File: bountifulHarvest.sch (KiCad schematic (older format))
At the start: 0 parts

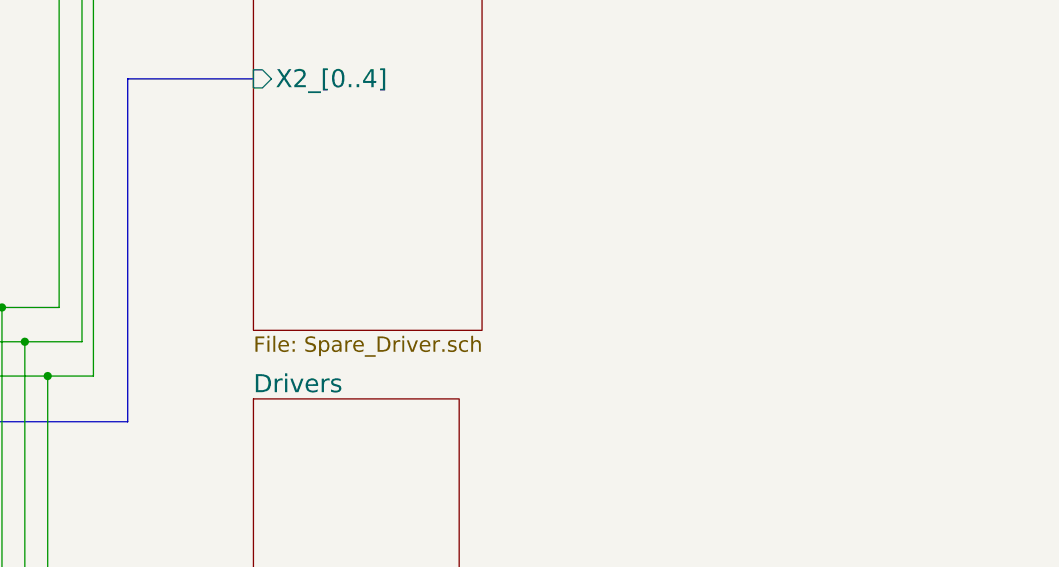
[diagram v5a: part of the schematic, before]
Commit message: Found error in stepper driver supply
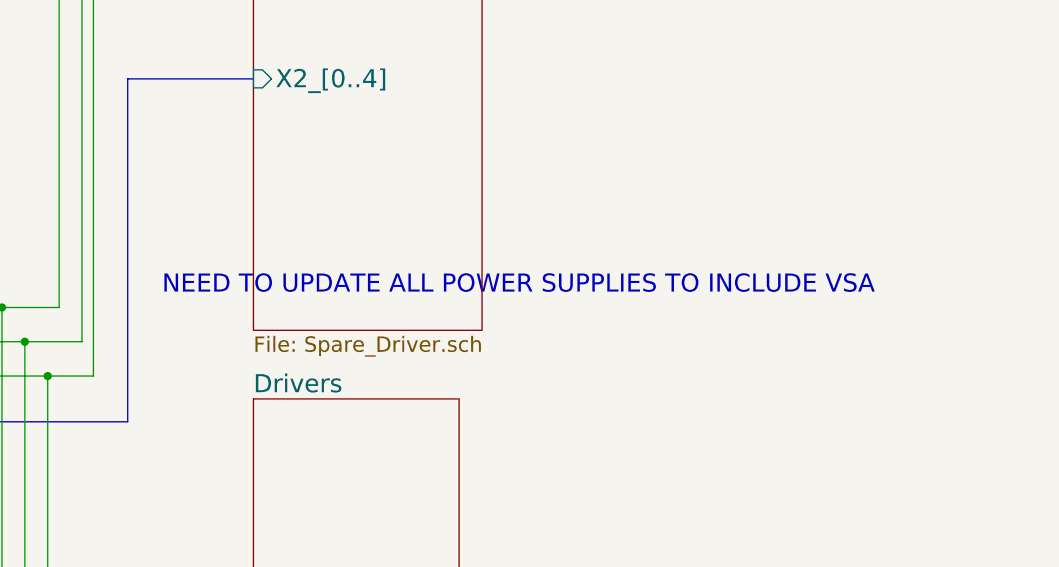
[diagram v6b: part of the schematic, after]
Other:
- note added: "NEED TO UPDATE ALL POWER SUPPLIES TO INCLUDE VSA"
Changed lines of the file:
@@
 EESchema Schematic File Version 4
-LIBS:bountifulHarvest-cache
-EELAYER 26 0
+EELAYER 30 0
 EELAYER END
 $Descr A4 11693 8268
@@
 Wire Wire Line
 	3850 6950 4350 6950
+Text Notes 9700 2750 0    79   ~ 0
+NEED TO UPDATE ALL POWER SUPPLIES TO INCLUDE VSA
 $EndSCHEMATC

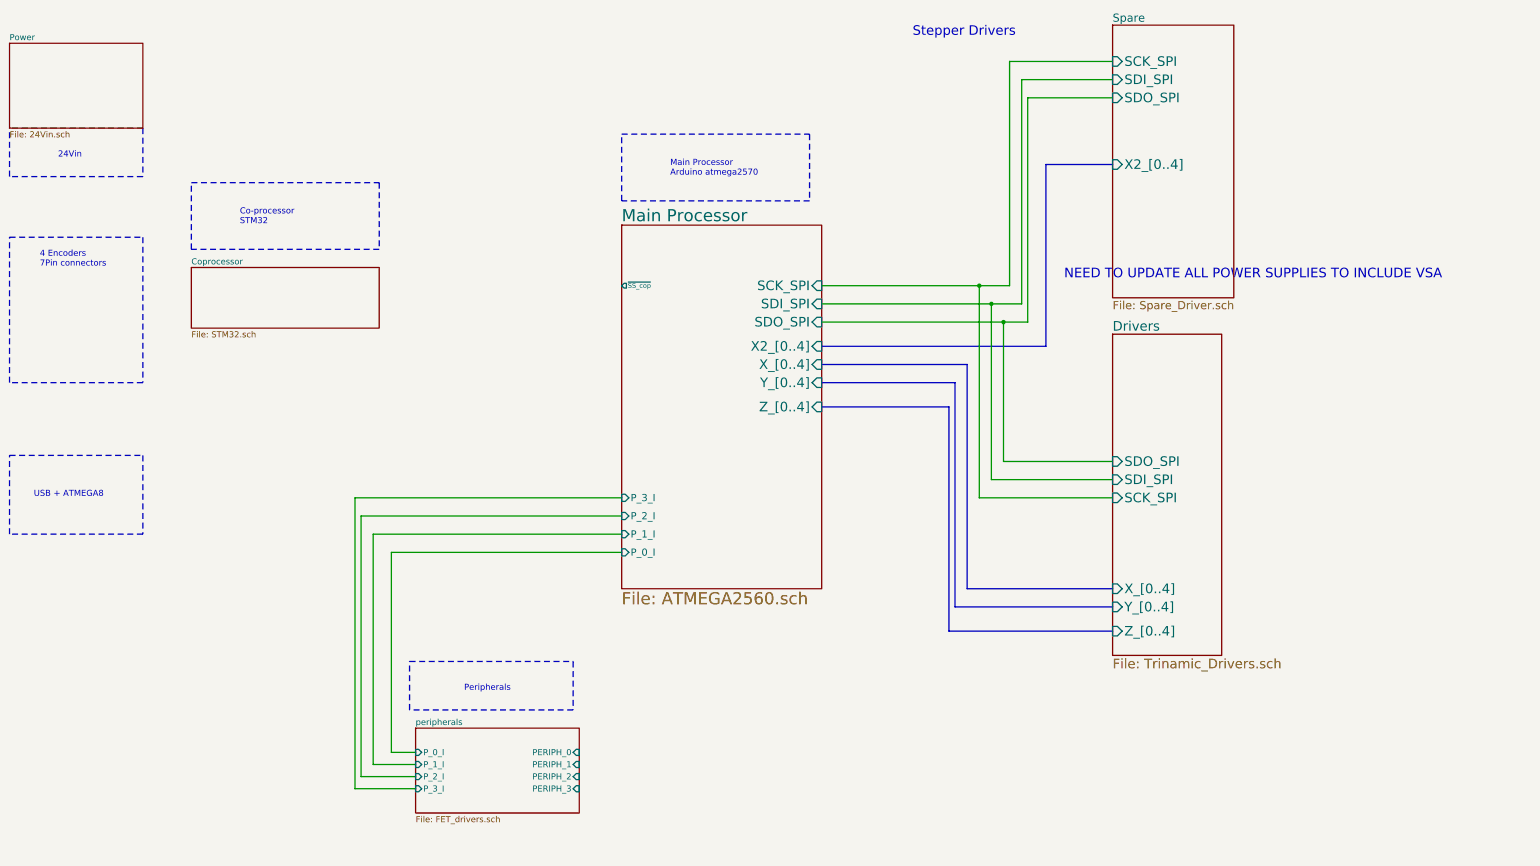
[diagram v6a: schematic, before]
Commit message: updated ATMEGA and regulators
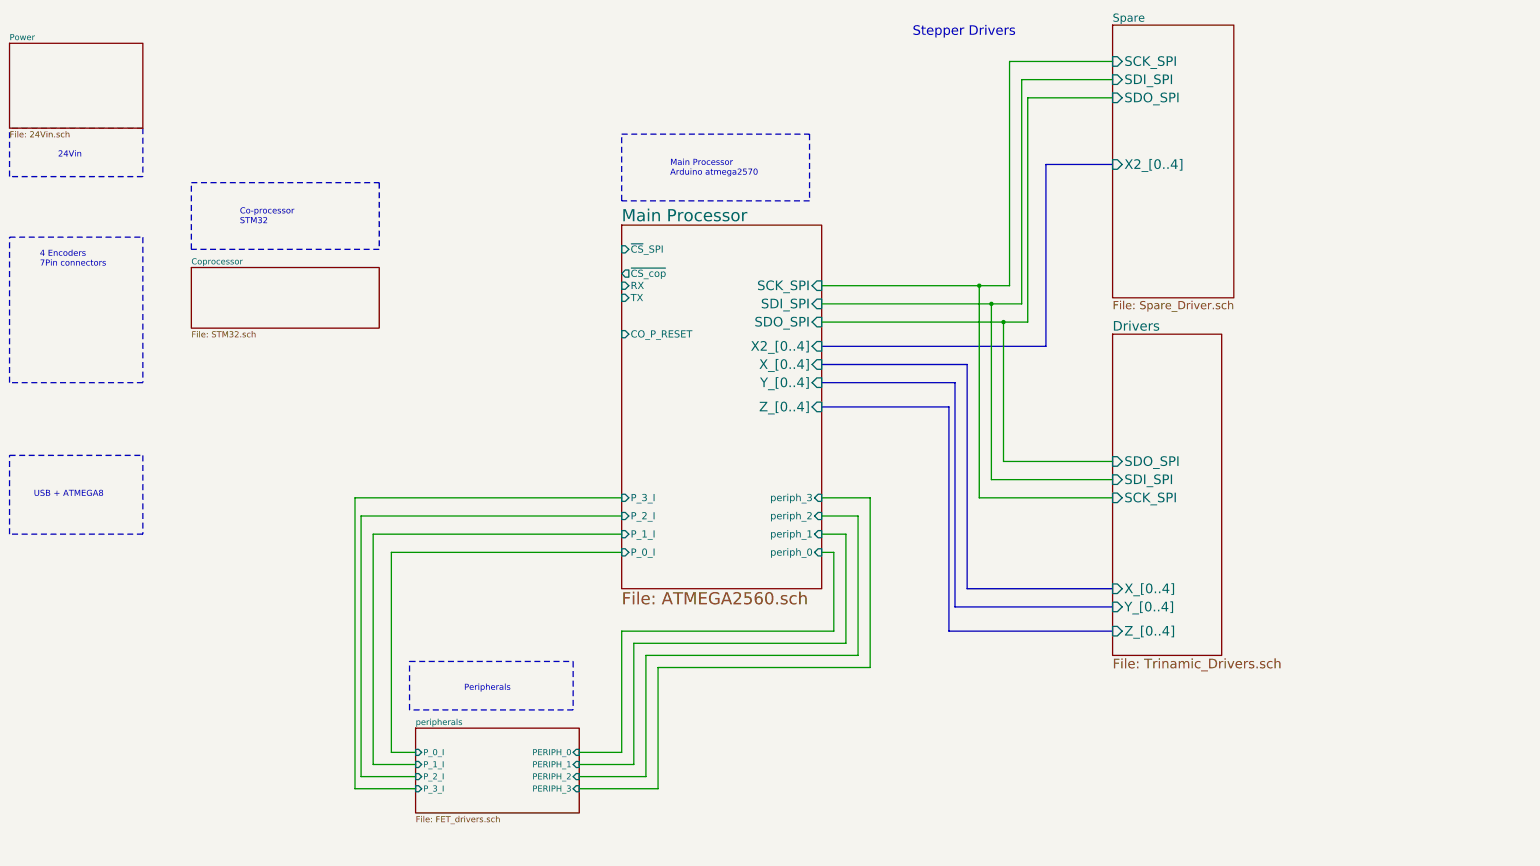
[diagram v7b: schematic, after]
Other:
- note removed: "NEED TO UPDATE ALL POWER SUPPLIES TO INCLUDE VSA"
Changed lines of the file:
@@
 F6 "Y_[0..4]" I R 7700 3600 79
 F7 "Z_[0..4]" I R 7700 3800 79
-F8 "~SS_cop" O L 6050 2800 39
-F9 "X2_[0..4]" I R 7700 3300 79
-F10 "P_0_I" I L 6050 5000 59
-F11 "P_1_I" I L 6050 4850 59
-F12 "P_2_I" I L 6050 4700 59
-F13 "P_3_I" I L 6050 4550 59
+F8 "X2_[0..4]" I R 7700 3300 79
+F9 "P_0_I" I L 6050 5000 59
+F10 "P_1_I" I L 6050 4850 59
+F11 "P_2_I" I L 6050 4700 59
+F12 "P_3_I" I L 6050 4550 59
+F13 "periph_0" I R 7700 5000 59
+F14 "periph_1" I R 7700 4850 59
+F15 "periph_2" I R 7700 4700 59
+F16 "periph_3" I R 7700 4550 59
+F17 "~CS_cop" O L 6050 2700 59
+F18 "TX" I L 6050 2900 59
+F19 "RX" I L 6050 2800 59
+F20 "~CS~_SPI" I L 6050 2500 59
+F21 "CO_P_RESET" I L 6050 3200 59
 $EndSheet
 Wire Wire Line
@@
 Wire Wire Line
 	3850 6950 4350 6950
-Text Notes 9700 2750 0    79   ~ 0
-NEED TO UPDATE ALL POWER SUPPLIES TO INCLUDE VSA
+Wire Wire Line
+	7700 5000 7800 5000
+Wire Wire Line
+	7800 5000 7800 5650
+Wire Wire Line
+	7800 5650 6050 5650
+Wire Wire Line
+	6050 5650 6050 6650
+Wire Wire Line
+	6050 6650 5700 6650
+Wire Wire Line
+	5700 6750 6150 6750
+Wire Wire Line
+	6150 6750 6150 5750
+Wire Wire Line
+	6150 5750 7900 5750
+Wire Wire Line
+	7900 5750 7900 4850
+Wire Wire Line
+	7900 4850 7700 4850
+Wire Wire Line
+	7700 4700 8000 4700
+Wire Wire Line
+	8000 4700 8000 5850
+Wire Wire Line
+	8000 5850 6250 5850
+Wire Wire Line
+	6250 5850 6250 6850
+Wire Wire Line
+	6250 6850 5700 6850
+Wire Wire Line
+	5700 6950 6350 6950
+Wire Wire Line
+	6350 6950 6350 5950
+Wire Wire Line
+	6350 5950 8100 5950
+Wire Wire Line
+	8100 5950 8100 4550
+Wire Wire Line
+	8100 4550 7700 4550
 $EndSCHEMATC

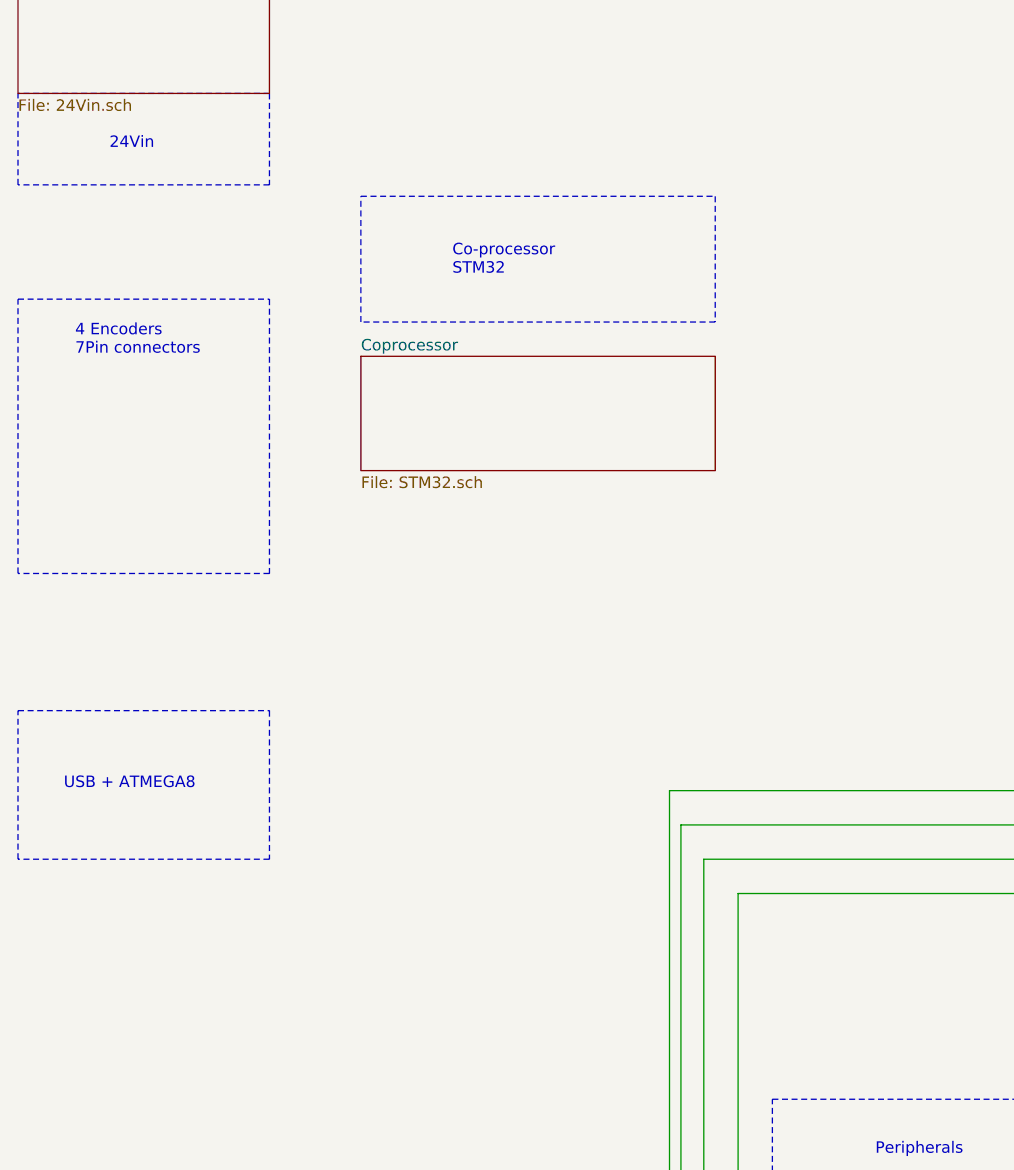
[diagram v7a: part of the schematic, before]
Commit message: added differential RX
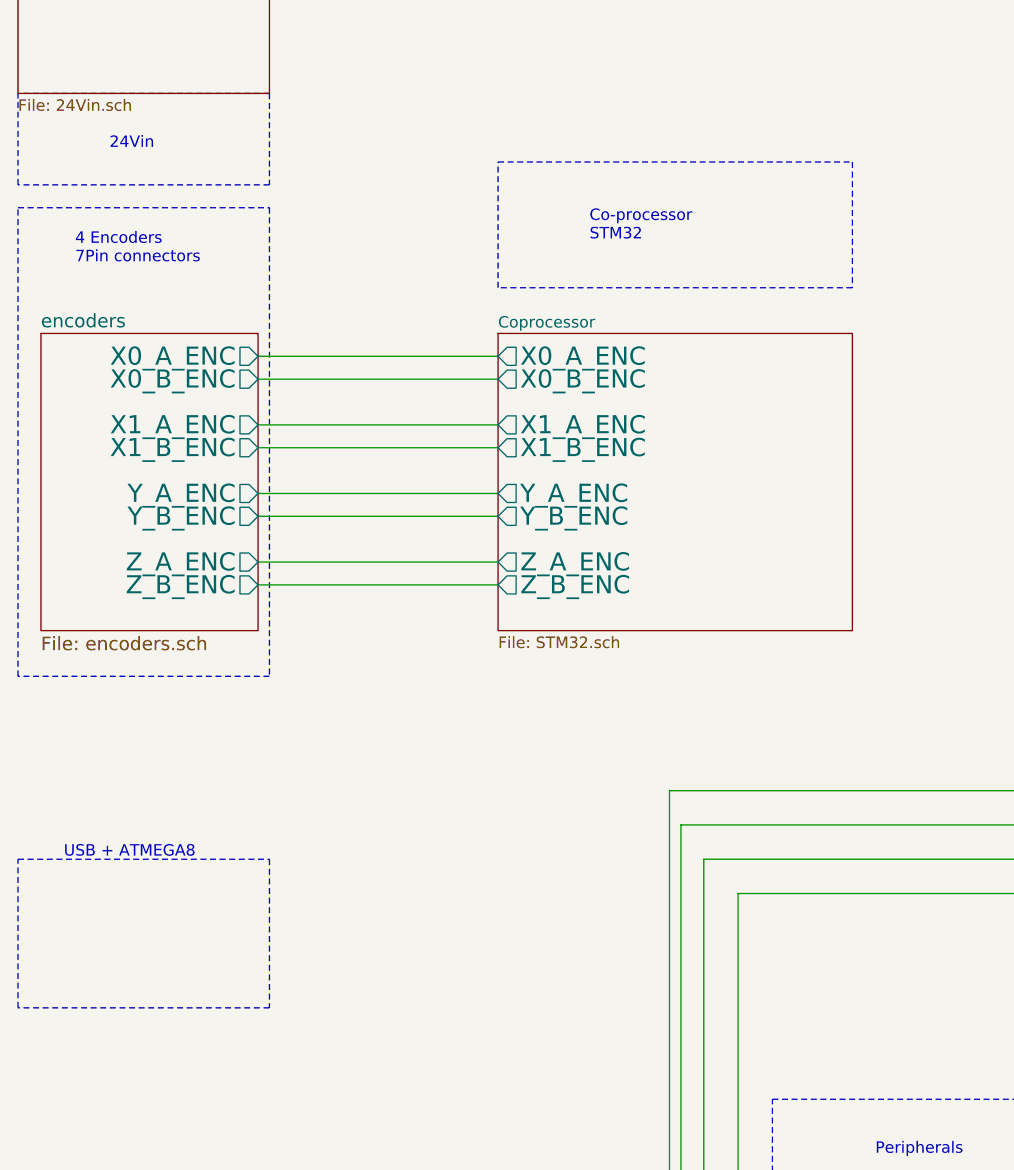
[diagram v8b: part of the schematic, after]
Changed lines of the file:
@@
 $Descr A4 11693 8268
 encoding utf-8
-Sheet 1 7
+Sheet 1 8
 Title "BountifulHarvest"
 Date ""
@@
 24Vin
 Wire Notes Line
-	1000 2400 2100 2400
-Wire Notes Line
-	2100 2400 2100 3600
-Wire Notes Line
-	2100 3600 1000 3600
-Wire Notes Line
-	1000 3600 1000 2400
-Text Notes 1250 2650 0    50   ~ 0
+	1000 2000 2100 2000
+Wire Notes Line
+	2100 2000 2100 4050
+Wire Notes Line
+	2100 4050 1000 4050
+Wire Notes Line
+	1000 4050 1000 2000
+Text Notes 1250 2250 0    50   ~ 0
 4 Encoders\n7Pin connectors\n
 Wire Notes Line
@@
 Main Processor\nArduino atmega2570
 Wire Notes Line
-	4050 1950 4050 2500
-Wire Notes Line
-	4050 2500 2500 2500
-Wire Notes Line
-	2500 2500 2500 1950
-Wire Notes Line
-	2500 1950 4050 1950
-Text Notes 2900 2300 0    50   ~ 0
+	4650 1800 4650 2350
+Wire Notes Line
+	4650 2350 3100 2350
+Wire Notes Line
+	3100 2350 3100 1800
+Wire Notes Line
+	3100 1800 4650 1800
+Text Notes 3500 2150 0    50   ~ 0
 Co-processor\nSTM32
 $Sheet
-S 2500 2650 1550 500
+S 3100 2550 1550 1300
 U 5EE7212D
 F0 "Coprocessor" 50
 F1 "STM32.sch" 50
+F2 "X0_A_ENC" O L 3100 2650 79
+F3 "X0_B_ENC" O L 3100 2750 79
+F4 "X1_A_ENC" O L 3100 2950 79
+F5 "X1_B_ENC" O L 3100 3050 79
+F6 "Y_A_ENC" O L 3100 3250 79
+F7 "Y_B_ENC" O L 3100 3350 79
+F8 "Z_A_ENC" O L 3100 3550 79
+F9 "Z_B_ENC" O L 3100 3650 79
 $EndSheet
 Wire Notes Line
 	4300 5900 5650 5900
 Wire Notes Line
-	1000 4200 2100 4200
-Wire Notes Line
-	2100 4200 2100 4850
-Wire Notes Line
-	2100 4850 1000 4850
-Wire Notes Line
-	1000 4850 1000 4200
-Text Notes 1200 4550 0    50   ~ 0
+	1000 4850 2100 4850
+Wire Notes Line
+	2100 4850 2100 5500
+Wire Notes Line
+	2100 5500 1000 5500
+Wire Notes Line
+	1000 5500 1000 4850
+Text Notes 1200 4850 0    50   ~ 0
 USB + ATMEGA8
 $Sheet
@@
 Wire Wire Line
 	8100 4550 7700 4550
+$Sheet
+S 1100 2550 950  1300
+U 62A6BDCF
+F0 "encoders" 59
+F1 "encoders.sch" 59
+F2 "X0_A_ENC" O R 2050 2650 79
+F3 "X0_B_ENC" O R 2050 2750 79
+F4 "X1_A_ENC" O R 2050 2950 79
+F5 "X1_B_ENC" O R 2050 3050 79
+F6 "Y_A_ENC" O R 2050 3250 79
+F7 "Y_B_ENC" O R 2050 3350 79
+F8 "Z_A_ENC" O R 2050 3550 79
+F9 "Z_B_ENC" O R 2050 3650 79
+$EndSheet
+Wire Wire Line
+	2050 2650 3100 2650
+Wire Wire Line
+	3100 2750 2050 2750
+Wire Wire Line
+	2050 2950 3100 2950
+Wire Wire Line
+	3100 3050 2050 3050
+Wire Wire Line
+	2050 3250 3100 3250
+Wire Wire Line
+	3100 3350 2050 3350
+Wire Wire Line
+	2050 3550 3100 3550
+Wire Wire Line
+	3100 3650 2050 3650
 $EndSCHEMATC
